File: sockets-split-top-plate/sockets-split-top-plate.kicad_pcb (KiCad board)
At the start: 2 copper layers, 137.9 x 85.2 mm, 0 parts

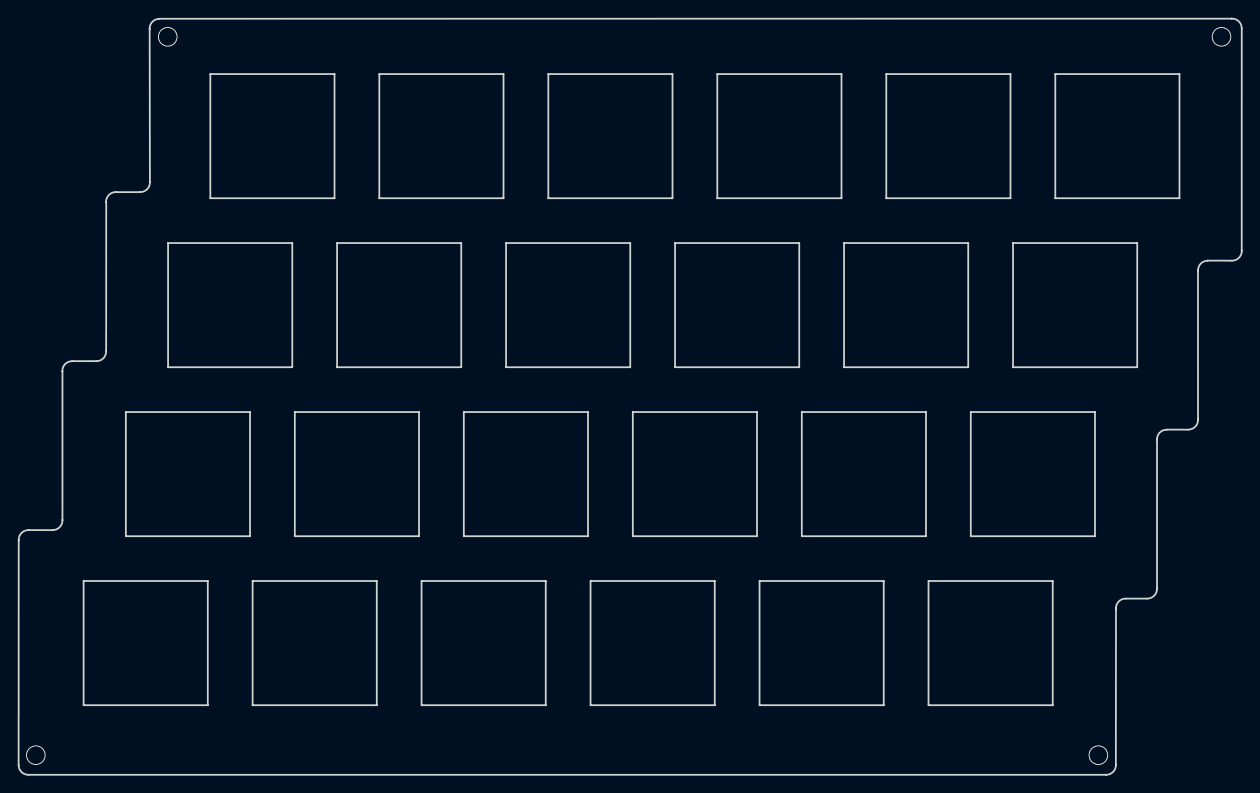
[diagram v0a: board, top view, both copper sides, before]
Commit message: Add solder layer & Fix document
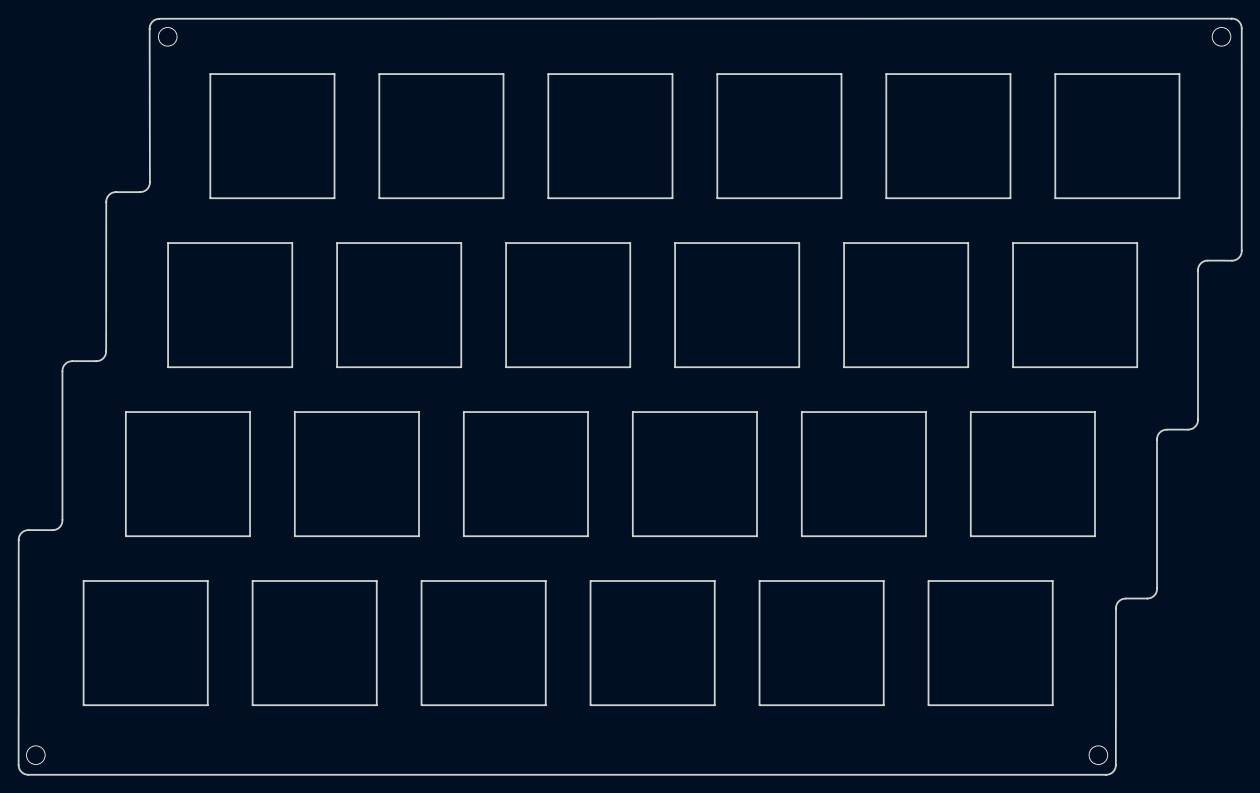
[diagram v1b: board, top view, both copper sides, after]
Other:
- outline, holes or cut-outs redrawn
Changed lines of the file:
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@@
   (general
     (thickness 1.6)
-    (drawings 130)
+    (drawings 132)
     (tracks 4)
     (zones 0)
@@
     (0 F.Cu signal)
     (31 B.Cu signal)
-    (32 B.Adhes user)
-    (33 F.Adhes user)
-    (34 B.Paste user)
-    (35 F.Paste user)
+    (32 B.Adhes user hide)
+    (33 F.Adhes user hide)
+    (34 B.Paste user hide)
+    (35 F.Paste user hide)
     (36 B.SilkS user)
     (37 F.SilkS user)
@@
     (39 F.Mask user)
     (40 Dwgs.User user hide)
-    (41 Cmts.User user)
-    (42 Eco1.User user)
-    (43 Eco2.User user)
+    (41 Cmts.User user hide)
+    (42 Eco1.User user hide)
+    (43 Eco2.User user hide)
     (44 Edge.Cuts user)
-    (45 Margin user)
-    (46 B.CrtYd user)
-    (47 F.CrtYd user)
-    (48 B.Fab user)
-    (49 F.Fab user)
+    (45 Margin user hide)
+    (46 B.CrtYd user hide)
+    (47 F.CrtYd user hide)
+    (48 B.Fab user hide)
+    (49 F.Fab user hide)
   )
   (setup
@@
     (uvia_drill 0.1)
   )
+  (dimension 85.160366 (width 0.3) (layer F.SilkS)
+    (gr_text "85.160 mm" (at 63.87 97.390183 270) (layer F.SilkS)
+      (effects (font (size 1.5 1.5) (thickness 0.3)))
+    )
+    (feature1 (pts (xy 85.45 139.970366) (xy 65.383579 139.970366)))
+    (feature2 (pts (xy 85.45 54.81) (xy 65.383579 54.81)))
+    (crossbar (pts (xy 65.97 54.81) (xy 65.97 139.970366)))
+    (arrow1a (pts (xy 65.97 139.970366) (xy 65.383579 138.843862)))
+    (arrow1b (pts (xy 65.97 139.970366) (xy 66.556421 138.843862)))
+    (arrow2a (pts (xy 65.97 54.81) (xy 65.383579 55.936504)))
+    (arrow2b (pts (xy 65.97 54.81) (xy 66.556421 55.936504)))
+  )
+  (dimension 137.77144 (width 0.3) (layer F.SilkS)
+    (gr_text "137.771 mm" (at 144.37572 165.15) (layer F.SilkS)
+      (effects (font (size 1.5 1.5) (thickness 0.3)))
+    )
+    (feature1 (pts (xy 213.26144 116.21) (xy 213.26144 163.636421)))
+    (feature2 (pts (xy 75.49 116.21) (xy 75.49 163.636421)))
+    (crossbar (pts (xy 75.49 163.05) (xy 213.26144 163.05)))
+    (arrow1a (pts (xy 213.26144 163.05) (xy 212.134936 163.636421)))
+    (arrow1b (pts (xy 213.26144 163.05) (xy 212.134936 162.463579)))
+    (arrow2a (pts (xy 75.49 163.05) (xy 76.616504 163.636421)))
+    (arrow2b (pts (xy 75.49 163.05) (xy 76.616504 162.463579)))
+  )
   (dimension 137.910305 (width 0.3) (layer Dwgs.User)
     (gr_text "137.910 mm" (at 144.310637 150.076341 359.8795174) (layer Dwgs.User)
@@
     (arrow2b (pts (xy 65.144868 139.736414) (xy 64.559639 138.609291)))
   )
-  (gr_arc (start 81.5 94.47) (end 81.5 93.38) (angle -93.34194386) (layer Edge.Cuts) (width 0.2))
+  (gr_arc (start 81.51 94.47) (end 81.51 93.38) (angle -93.34194386) (layer Edge.Cuts) (width 0.2))
   (gr_arc (start 84.251854 92.283541) (end 84.251854 93.373541) (angle -93.34194386) (layer Edge.Cuts) (width 0.2))
-  (gr_arc (start 86.428146 75.406459) (end 86.428146 74.316459) (angle -93.34194386) (layer Edge.Cuts) (width 0.2))
+  (gr_arc (start 86.448146 75.406459) (end 86.448146 74.316459) (angle -93.34194386) (layer Edge.Cuts) (width 0.2))
   (gr_arc (start 89.191854 73.223541) (end 89.191854 74.313541) (angle -93.34194386) (layer Edge.Cuts) (width 0.2))
   (gr_arc (start 91.338146 55.876459) (end 91.338146 54.786459) (angle -93.34194386) (layer Edge.Cuts) (width 0.2))
   (gr_arc (start 212.263541 55.848146) (end 213.353541 55.848146) (angle -93.34194386) (layer Edge.Cuts) (width 0.2))
-  (gr_arc (start 209.528146 83.136459) (end 209.528146 82.046459) (angle -93.34194386) (layer Edge.Cuts) (width 0.2))
+  (gr_arc (start 209.518146 83.126459) (end 209.518146 82.036459) (angle -93.34194386) (layer Edge.Cuts) (width 0.2))
   (gr_arc (start 212.27 80.953541) (end 212.27 82.043541) (angle -93.34194386) (layer Edge.Cuts) (width 0.2))
   (gr_arc (start 204.898146 102.19) (end 204.898146 101.1) (angle -93.34194386) (layer Edge.Cuts) (width 0.2))
   (gr_arc (start 207.341854 99.993541) (end 207.341854 101.083541) (angle -93.34194386) (layer Edge.Cuts) (width 0.2))
-  (gr_arc (start 202.711854 119.043541) (end 202.711854 120.133541) (angle -93.34194386) (layer Edge.Cuts) (width 0.2))
+  (gr_arc (start 202.72 119.04) (end 202.72 120.13) (angle -93.34194386) (layer Edge.Cuts) (width 0.2))
   (gr_arc (start 200.27 121.23) (end 200.27 120.14) (angle -93.34194386) (layer Edge.Cuts) (width 0.2))
   (gr_arc (start 198.08 138.91) (end 198.08 140) (angle -90) (layer Edge.Cuts) (width 0.2))
   (gr_arc (start 76.57 138.91) (end 75.48 138.91) (angle -90) (layer Edge.Cuts) (width 0.2))
-  (gr_arc (start 79.33 111.32) (end 79.33 112.41) (angle -93.3) (layer Edge.Cuts) (width 0.2))
+  (gr_arc (start 79.33 111.33) (end 79.33 112.42) (angle -93.3) (layer Edge.Cuts) (width 0.2))
   (gr_arc (start 76.58 113.51) (end 76.58 112.42) (angle -93.3) (layer Edge.Cuts) (width 0.2))
   (gr_line (start 149.190274 75.006998) (end 135.191128 75.006998) (layer Edge.Cuts) (width 0.2))
@@
   (gr_line (start 201.577774 94.056998) (end 187.578973 94.056998) (layer Edge.Cuts) (width 0.2))
   (gr_line (start 130.140446 75.006998) (end 116.141128 75.006998) (layer Edge.Cuts) (width 0.2))
-  (gr_line (start 80.421 94.488324) (end 80.419622 111.307452) (layer Edge.Cuts) (width 0.2))
+  (gr_line (start 80.421 94.533541) (end 80.421 111.267255) (layer Edge.Cuts) (width 0.2))
   (gr_line (start 81.537211 93.372113) (end 84.229898 93.372113) (layer Edge.Cuts) (width 0.2))
   (gr_line (start 182.527774 80.058886) (end 182.527774 94.056998) (layer Edge.Cuts) (width 0.2))
@@
   (gr_line (start 182.527774 94.056998) (end 168.528284 94.056998) (layer Edge.Cuts) (width 0.2))
   (gr_line (start 168.528284 94.056998) (end 168.528284 80.058886) (layer Edge.Cuts) (width 0.2))
-  (gr_line (start 200.300332 120.142055) (end 202.692607 120.142055) (layer Edge.Cuts) (width 0.2))
+  (gr_line (start 200.300332 120.13) (end 202.72 120.13) (layer Edge.Cuts) (width 0.2))
   (gr_line (start 187.578973 80.058886) (end 201.577774 80.058886) (layer Edge.Cuts) (width 0.2))
-  (gr_line (start 203.808818 102.206716) (end 203.808818 119.025844) (layer Edge.Cuts) (width 0.2))
+  (gr_line (start 203.808818 102.206716) (end 203.808818 118.976459) (layer Edge.Cuts) (width 0.2))
   (gr_line (start 209.545591 82.040505) (end 212.241033 82.043261) (layer Edge.Cuts) (width 0.2))
   (gr_line (start 204.925028 101.090505) (end 207.314547 101.094639) (layer Edge.Cuts) (width 0.2))
@@
   (gr_line (start 212.244478 54.763445) (end 91.366413 54.774813) (layer Edge.Cuts) (width 0.2))
   (gr_line (start 76.607796 140.000551) (end 198.066532 140.000551) (layer Edge.Cuts) (width 0.2))
-  (gr_line (start 213.36 55.88) (end 213.357244 80.92705) (layer Edge.Cuts) (width 0.2))
+  (gr_line (start 213.36 55.88) (end 213.357244 80.89) (layer Edge.Cuts) (width 0.2))
   (via (at 211.08 56.81) (size 2.2) (drill 2) (layers F.Cu B.Cu) (net 0))
   (via (at 197.2 137.79) (size 2.2) (drill 2) (layers F.Cu B.Cu) (net 0))

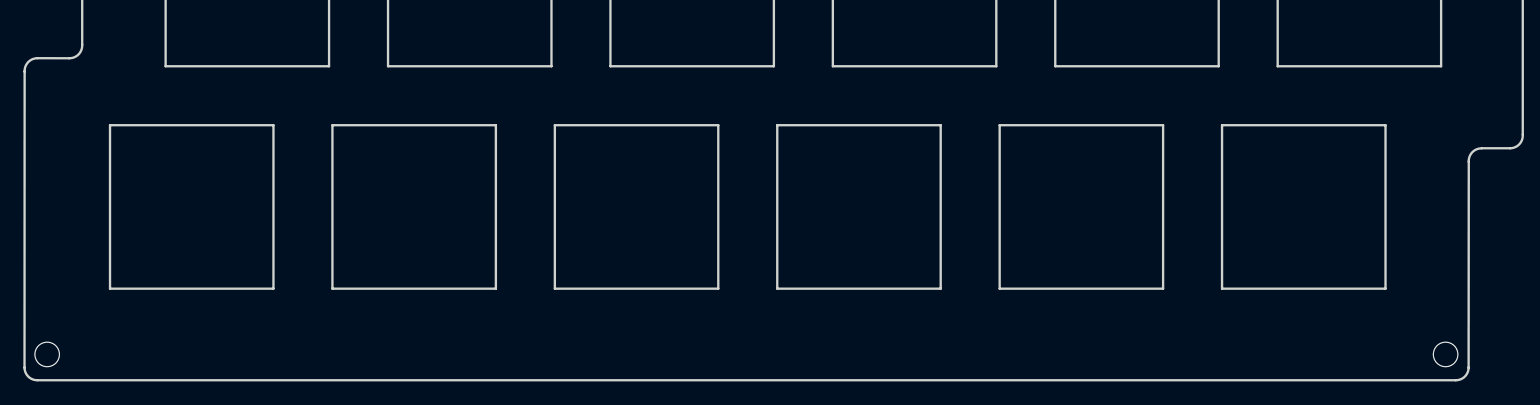
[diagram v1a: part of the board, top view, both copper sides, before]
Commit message: 一発で生産できなかったので、pcbの修正
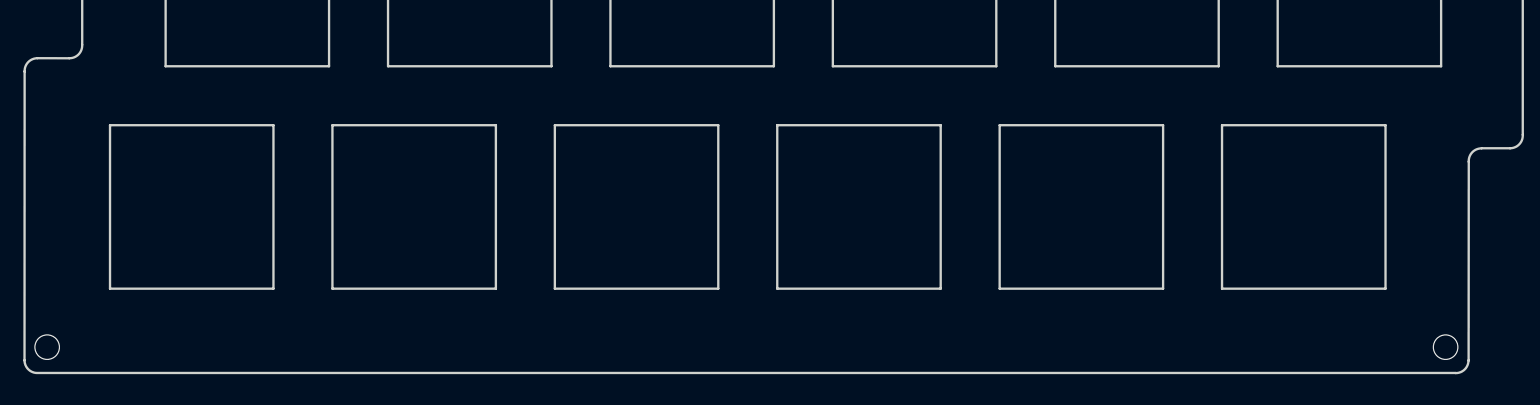
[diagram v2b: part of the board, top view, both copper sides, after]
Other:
- board size 137.9 x 85.2 mm -> 137.9 x 84.6 mm
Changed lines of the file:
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@@
   (general
     (thickness 1.6)
-    (drawings 132)
+    (drawings 140)
     (tracks 4)
     (zones 0)
@@
       (drillshape 0)
       (scaleselection 1)
-      (outputdirectory "../../../../Desktop/sockets-split-1.1/sockets-split-top/"))
+      (outputdirectory "../../../../Desktop/sockets-split-1.2/sockets-split-top/"))
   )
   (net 0 "")
@@
     (uvia_drill 0.1)
   )
-  (dimension 85.160366 (width 0.3) (layer F.SilkS)
-    (gr_text "85.160 mm" (at 63.87 97.390183 270) (layer F.SilkS)
-      (effects (font (size 1.5 1.5) (thickness 0.3)))
-    )
-    (feature1 (pts (xy 85.45 139.970366) (xy 65.383579 139.970366)))
-    (feature2 (pts (xy 85.45 54.81) (xy 65.383579 54.81)))
-    (crossbar (pts (xy 65.97 54.81) (xy 65.97 139.970366)))
-    (arrow1a (pts (xy 65.97 139.970366) (xy 65.383579 138.843862)))
-    (arrow1b (pts (xy 65.97 139.970366) (xy 66.556421 138.843862)))
-    (arrow2a (pts (xy 65.97 54.81) (xy 65.383579 55.936504)))
-    (arrow2b (pts (xy 65.97 54.81) (xy 66.556421 55.936504)))
+  (gr_circle (center 211.07925 56.81) (end 212.28 56.81) (layer F.Mask) (width 0.2))
+  (gr_circle (center 211.07925 56.81) (end 212.28 56.81) (layer B.Mask) (width 0.2))
+  (gr_circle (center 197.19925 137.17) (end 198.4 137.17) (layer B.Mask) (width 0.2))
+  (gr_circle (center 197.19925 137.17) (end 198.4 137.17) (layer F.Mask) (width 0.2))
+  (gr_circle (center 77.42 137.17) (end 78.62075 137.17) (layer B.Mask) (width 0.2))
+  (gr_circle (center 77.42 137.17) (end 78.62075 137.17) (layer F.Mask) (width 0.2))
+  (gr_circle (center 92.27925 56.8) (end 93.48 56.8) (layer B.Mask) (width 0.2))
+  (gr_circle (center 92.289251 56.81) (end 93.490001 56.81) (layer F.Mask) (width 0.2))
+  (dimension 84.605111 (width 0.3) (layer F.SilkS)
+    (gr_text "84.605 mm" (at 51.74 97.072555 270) (layer F.SilkS)
+      (effects (font (size 1.5 1.5) (thickness 0.3)))
+    )
+    (feature1 (pts (xy 97.55 139.375111) (xy 53.253579 139.375111)))
+    (feature2 (pts (xy 97.55 54.77) (xy 53.253579 54.77)))
+    (crossbar (pts (xy 53.84 54.77) (xy 53.84 139.375111)))
+    (arrow1a (pts (xy 53.84 139.375111) (xy 53.253579 138.248607)))
+    (arrow1b (pts (xy 53.84 139.375111) (xy 54.426421 138.248607)))
+    (arrow2a (pts (xy 53.84 54.77) (xy 53.253579 55.896504)))
+    (arrow2b (pts (xy 53.84 54.77) (xy 54.426421 55.896504)))
   )
   (dimension 137.77144 (width 0.3) (layer F.SilkS)
@@
   (gr_arc (start 202.72 119.04) (end 202.72 120.13) (angle -93.34194386) (layer Edge.Cuts) (width 0.2))
   (gr_arc (start 200.27 121.23) (end 200.27 120.14) (angle -93.34194386) (layer Edge.Cuts) (width 0.2))
-  (gr_arc (start 198.08 138.91) (end 198.08 140) (angle -90) (layer Edge.Cuts) (width 0.2))
-  (gr_arc (start 76.57 138.91) (end 75.48 138.91) (angle -90) (layer Edge.Cuts) (width 0.2))
+  (gr_arc (start 198.07 138.3) (end 198.07 139.39) (angle -90) (layer Edge.Cuts) (width 0.2))
+  (gr_arc (start 76.57 138.29) (end 75.48 138.29) (angle -90) (layer Edge.Cuts) (width 0.2))
   (gr_arc (start 79.33 111.33) (end 79.33 112.42) (angle -93.3) (layer Edge.Cuts) (width 0.2))
   (gr_arc (start 76.58 113.51) (end 76.58 112.42) (angle -93.3) (layer Edge.Cuts) (width 0.2))
@@
   (gr_line (start 196.815274 99.108886) (end 196.815274 113.10717) (layer Edge.Cuts) (width 0.2))
   (gr_line (start 130.428628 80.058886) (end 144.427774 80.058886) (layer Edge.Cuts) (width 0.2))
-  (gr_line (start 199.184121 121.258266) (end 199.17 138.94) (layer Edge.Cuts) (width 0.2))
-  (gr_line (start 75.490207 113.531606) (end 75.48 138.92) (layer Edge.Cuts) (width 0.2))
+  (gr_line (start 199.184121 121.258266) (end 199.17 138.317) (layer Edge.Cuts) (width 0.2))
+  (gr_line (start 75.490207 113.531606) (end 75.48 138.297) (layer Edge.Cuts) (width 0.2))
   (gr_line (start 86.473172 74.320735) (end 89.16448 74.320735) (layer Edge.Cuts) (width 0.2))
   (gr_line (start 163.477774 80.058886) (end 163.477774 94.056998) (layer Edge.Cuts) (width 0.2))
@@
   (gr_line (start 208.42938 83.156716) (end 208.430758 99.978428) (layer Edge.Cuts) (width 0.2))
   (gr_line (start 212.244478 54.763445) (end 91.366413 54.774813) (layer Edge.Cuts) (width 0.2))
-  (gr_line (start 76.607796 140.000551) (end 198.066532 140.000551) (layer Edge.Cuts) (width 0.2))
+  (gr_line (start 76.607796 139.377551) (end 198.066532 139.377551) (layer Edge.Cuts) (width 0.2))
   (gr_line (start 213.36 55.88) (end 213.357244 80.89) (layer Edge.Cuts) (width 0.2))
   (via (at 211.08 56.81) (size 2.2) (drill 2) (layers F.Cu B.Cu) (net 0))
-  (via (at 197.2 137.79) (size 2.2) (drill 2) (layers F.Cu B.Cu) (net 0))
-  (via (at 77.42 137.79) (size 2.2) (drill 2) (layers F.Cu B.Cu) (net 0))
+  (via (at 197.2 137.167) (size 2.2) (drill 2) (layers F.Cu B.Cu) (net 0))
+  (via (at 77.42 137.167) (size 2.2) (drill 2) (layers F.Cu B.Cu) (net 0))
   (via (at 92.29 56.81) (size 2.2) (drill 2) (layers F.Cu B.Cu) (net 0))
 )
